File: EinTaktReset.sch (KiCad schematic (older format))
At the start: 59 parts, among them IC1 74LS624, J1 3PinTerminalBlocktg, J2 3PinTerminalBlocktg, P1 CONN_02X10, P4 CONN_02X10, SW1 SPST, SW10 SPST, SW11 SPST, SW12 SPST, SW13 SPST, SW2 SWITCH_INV, SW3 SPST, SW4 SPST, SW5 SPST, SW6 SWITCH_INV, SW7 SPST, SW8 SPST, SW9 SPST, U1 74LS132, U2 74540En, U3 74HCT541_PWR, U4 74LS32, U5 74LS00, U6 74LS132

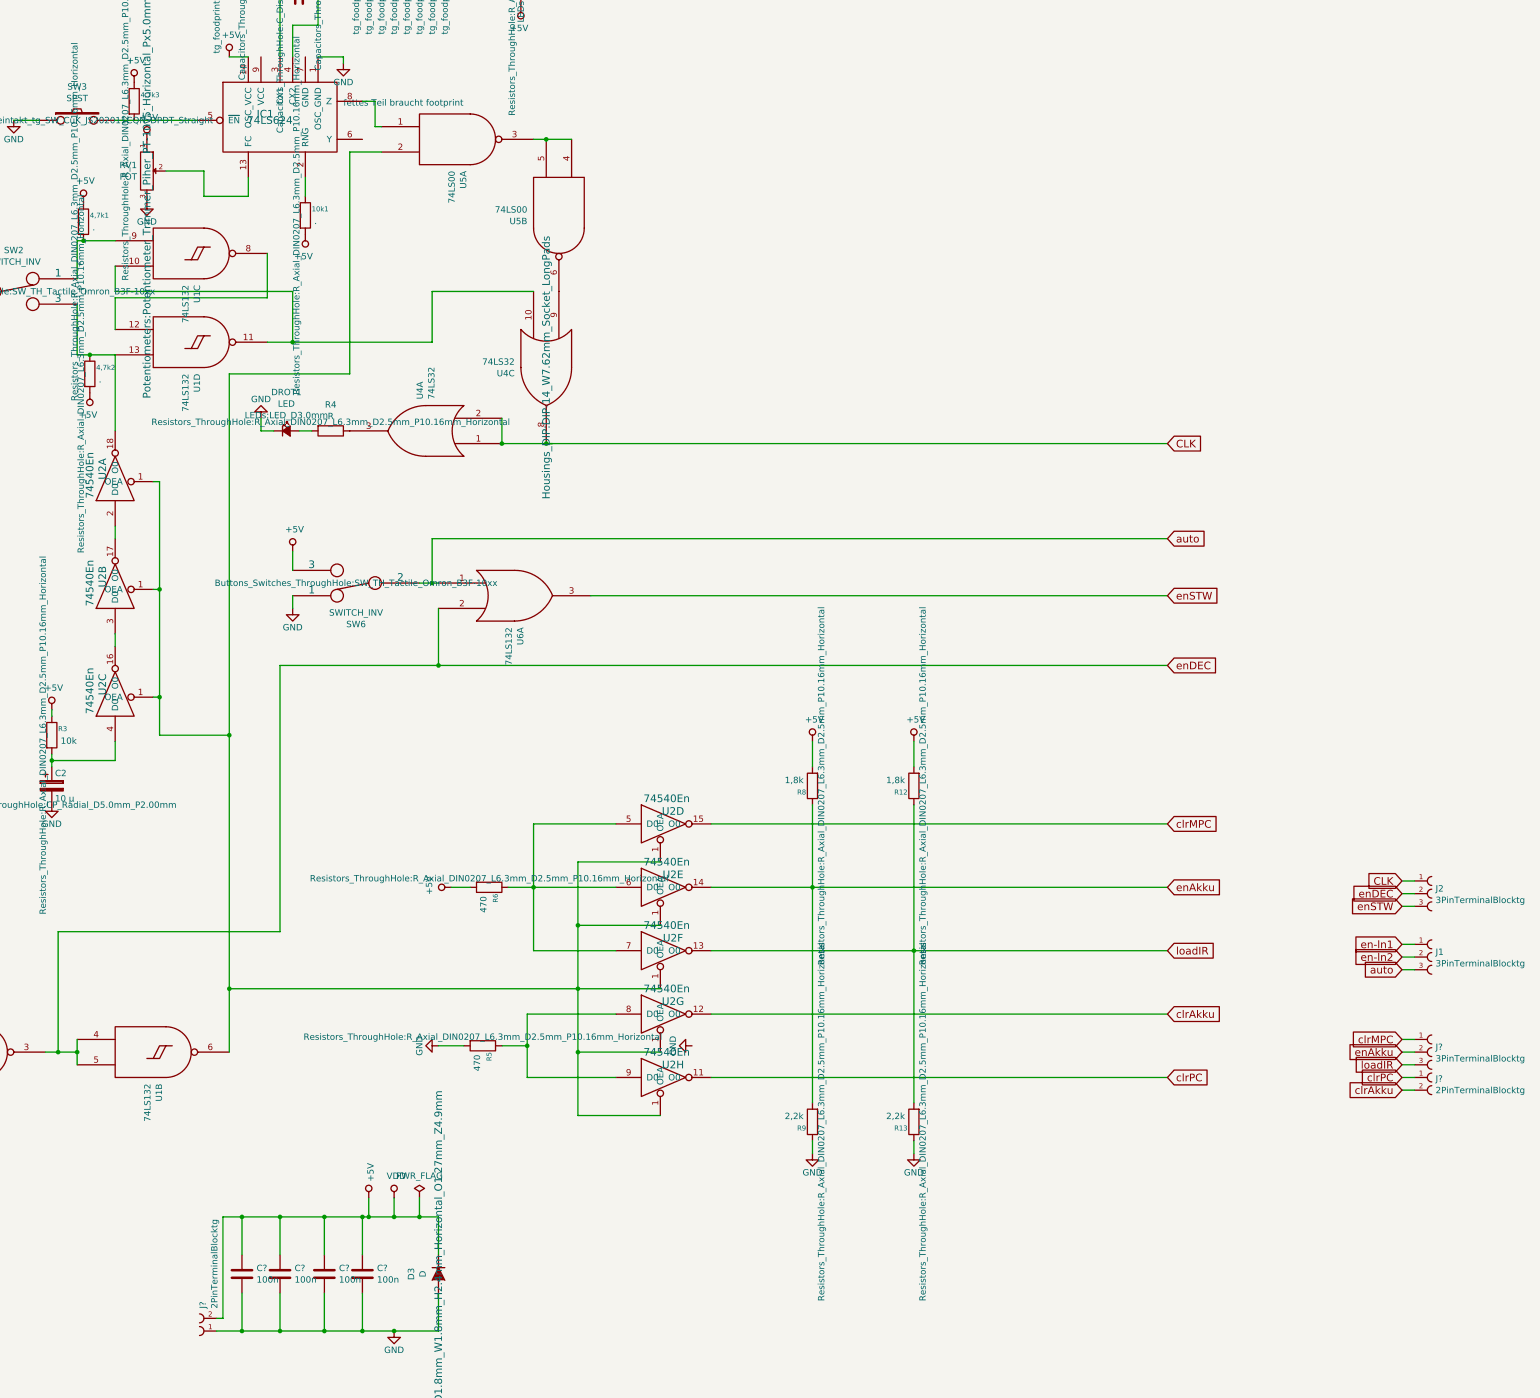
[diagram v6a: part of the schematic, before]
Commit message: pcb gelayoutet, Libraries benannt, todo.txt geändert!
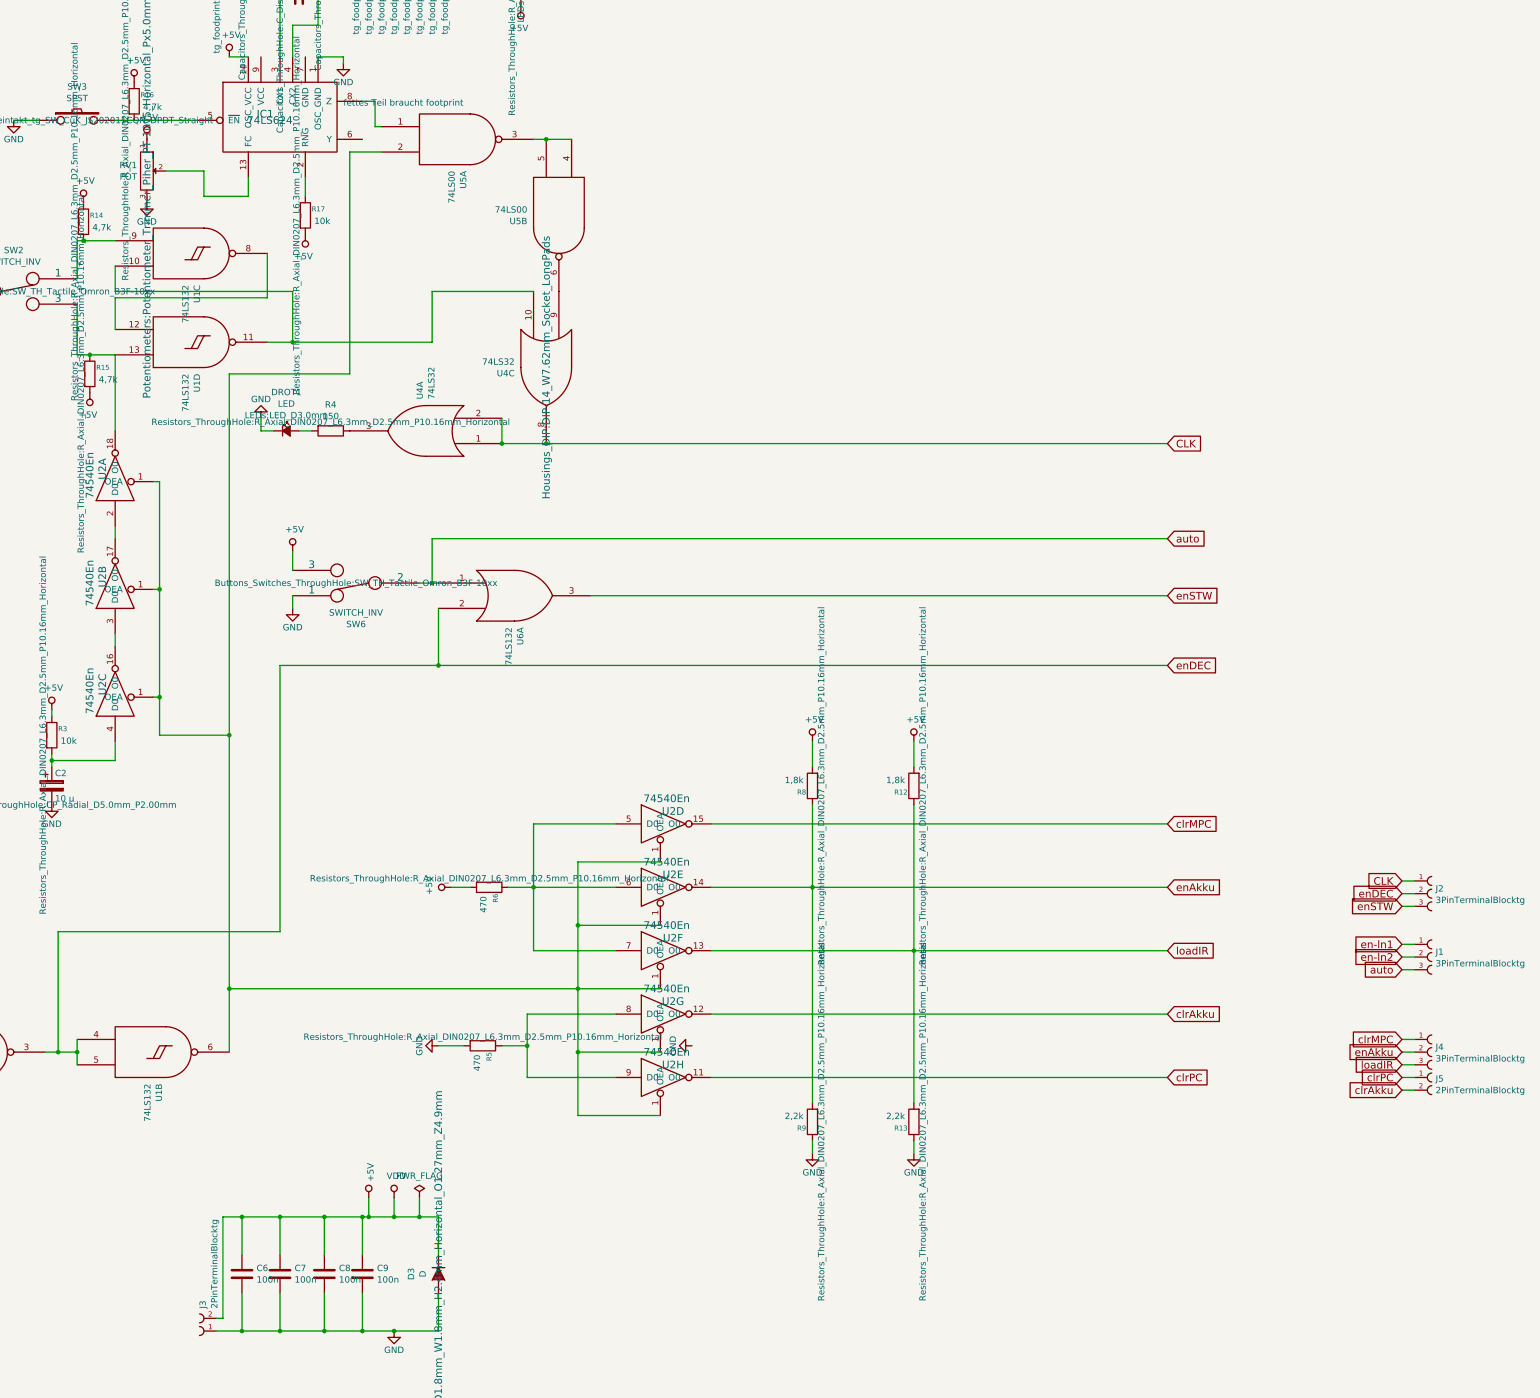
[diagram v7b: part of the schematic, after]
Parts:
- R14: renamed from 4,7k1; value . -> 4,7k
- R15: renamed from 4,7k2; value . -> 4,7k
- R16: renamed from 4,7k3; value . -> 4,7k
- R17: renamed from 10k1; value . -> 10k
- R4: value R -> 150
- gave numbers to parts that had none: 7
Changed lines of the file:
@@
 $EndComp
 $Comp
-L device:R 4,7k3
+L device:R R16
 U 1 1 5845B97A
 P 2500 5800
-F 0 "4,7k3" H 2550 5850 39  0000 L CNN
-F 1 "." H 2570 5755 50  0000 L CNN
+F 0 "R16" H 2550 5850 39  0000 L CNN
+F 1 "4,7k" H 2570 5755 50  0000 L CNN
 F 2 "Resistors_ThroughHole:R_Axial_DIN0207_L6.3mm_D2.5mm_P10.16mm_Horizontal" V 2430 5800 50  0000 C CNN
 F 3 "" H 2500 5800 50  0000 C CNN
@@
 $EndComp
 $Comp
-L device:R 10k1
+L device:R R17
 U 1 1 5845CFFB
 P 3850 6700
-F 0 "10k1" H 3900 6750 39  0000 L CNN
-F 1 "." H 3920 6655 50  0000 L CNN
+F 0 "R17" H 3900 6750 39  0000 L CNN
+F 1 "10k" H 3920 6655 50  0000 L CNN
 F 2 "Resistors_ThroughHole:R_Axial_DIN0207_L6.3mm_D2.5mm_P10.16mm_Horizontal" V 3780 6700 50  0000 C CNN
 F 3 "" H 3850 6700 50  0000 C CNN
@@
 $EndComp
 $Comp
-L device:R 4,7k2
+L device:R R15
 U 1 1 5845E30F
 P 2150 7950
-F 0 "4,7k2" H 2200 8000 39  0000 L CNN
-F 1 "." H 2220 7905 50  0000 L CNN
+F 0 "R15" H 2200 8000 39  0000 L CNN
+F 1 "4,7k" H 2220 7905 50  0000 L CNN
 F 2 "Resistors_ThroughHole:R_Axial_DIN0207_L6.3mm_D2.5mm_P10.16mm_Horizontal" V 2080 7950 50  0000 C CNN
 F 3 "" H 2150 7950 50  0000 C CNN
@@
 $EndComp
 $Comp
-L device:R 4,7k1
+L device:R R14
 U 1 1 5845F8A9
 P 2100 6750
-F 0 "4,7k1" H 2150 6800 39  0000 L CNN
-F 1 "." H 2170 6705 50  0000 L CNN
+F 0 "R14" H 2150 6800 39  0000 L CNN
+F 1 "4,7k" H 2170 6705 50  0000 L CNN
 F 2 "Resistors_ThroughHole:R_Axial_DIN0207_L6.3mm_D2.5mm_P10.16mm_Horizontal" V 2030 6750 50  0000 C CNN
 F 3 "" H 2100 6750 50  0000 C CNN
@@
 P 4050 8400
 F 0 "R4" V 3843 8400 50  0000 C CNN
-F 1 "R" V 3934 8400 50  0000 C CNN
+F 1 "150" V 3934 8400 50  0000 C CNN
 F 2 "Resistors_ThroughHole:R_Axial_DIN0207_L6.3mm_D2.5mm_P10.16mm_Horizontal" V 3980 8400 50  0000 C CNN
 F 3 "" H 4050 8400 50  0000 C CNN
@@
 	5750 8500 10650 8500
 $Comp
-L 2PinTerminalBlocktg:2PinTerminalBlocktg J?
+L 2PinTerminalBlocktg:2PinTerminalBlocktg J5
 U 1 1 5AC4DB91
 P 12800 13500
-F 0 "J?" H 12765 13490 50  0000 L CNN
+F 0 "J5" H 12765 13490 50  0000 L CNN
 F 1 "2PinTerminalBlocktg" H 12765 13399 50  0000 L CNN
 F 2 "2PinTerminalBlocktg" H 12800 13500 50  0001 L BNN
@@
 $EndComp
 $Comp
-L 3PinTerminalBlocktg:3PinTerminalBlocktg J?
+L 3PinTerminalBlocktg:3PinTerminalBlocktg J4
 U 1 1 5AC4DD64
 P 12800 13300
-F 0 "J?" H 12765 13340 50  0000 L CNN
+F 0 "J4" H 12765 13340 50  0000 L CNN
 F 1 "3PinTerminalBlocktg" H 12765 13249 50  0000 L CNN
 F 2 "3PinTerminalBlocktg" H 12800 13300 50  0001 L BNN
@@
 	12600 13600 12500 13600
 $Comp
-L 2PinTerminalBlocktg:2PinTerminalBlocktg J?
+L 2PinTerminalBlocktg:2PinTerminalBlocktg J3
 U 1 1 5ADB7E0E
 P 2950 15500
-F 0 "J?" V 2858 15323 50  0000 R CNN
+F 0 "J3" V 2858 15323 50  0000 R CNN
 F 1 "2PinTerminalBlocktg" V 2767 15323 50  0000 R CNN
 F 2 "2PinTerminalBlocktg" H 2950 15500 50  0001 L BNN
@@
 	4900 15500 4900 15200
 $Comp
-L bonsai:C C?
+L bonsai:C C9
 U 1 1 5AFD86A4
 P 4300 15050
-F 0 "C?" H 4415 15096 50  0000 L CNN
+F 0 "C9" H 4415 15096 50  0000 L CNN
 F 1 "100n" H 4415 15005 50  0000 L CNN
 F 2 "" H 4338 14900 30  0000 C CNN
@@
 $EndComp
 $Comp
-L bonsai:C C?
+L bonsai:C C8
 U 1 1 5AFEAAC4
 P 4000 15050
-F 0 "C?" H 4115 15096 50  0000 L CNN
+F 0 "C8" H 4115 15096 50  0000 L CNN
 F 1 "100n" H 4115 15005 50  0000 L CNN
 F 2 "" H 4038 14900 30  0000 C CNN
@@
 $EndComp
 $Comp
-L bonsai:C C?
+L bonsai:C C7
 U 1 1 5AFEABD4
 P 3650 15050
-F 0 "C?" H 3765 15096 50  0000 L CNN
+F 0 "C7" H 3765 15096 50  0000 L CNN
 F 1 "100n" H 3765 15005 50  0000 L CNN
 F 2 "" H 3688 14900 30  0000 C CNN
@@
 $EndComp
 $Comp
-L bonsai:C C?
+L bonsai:C C6
 U 1 1 5AFEACE5
 P 3350 15050
-F 0 "C?" H 3465 15096 50  0000 L CNN
+F 0 "C6" H 3465 15096 50  0000 L CNN
 F 1 "100n" H 3465 15005 50  0000 L CNN
 F 2 "" H 3388 14900 30  0000 C CNN

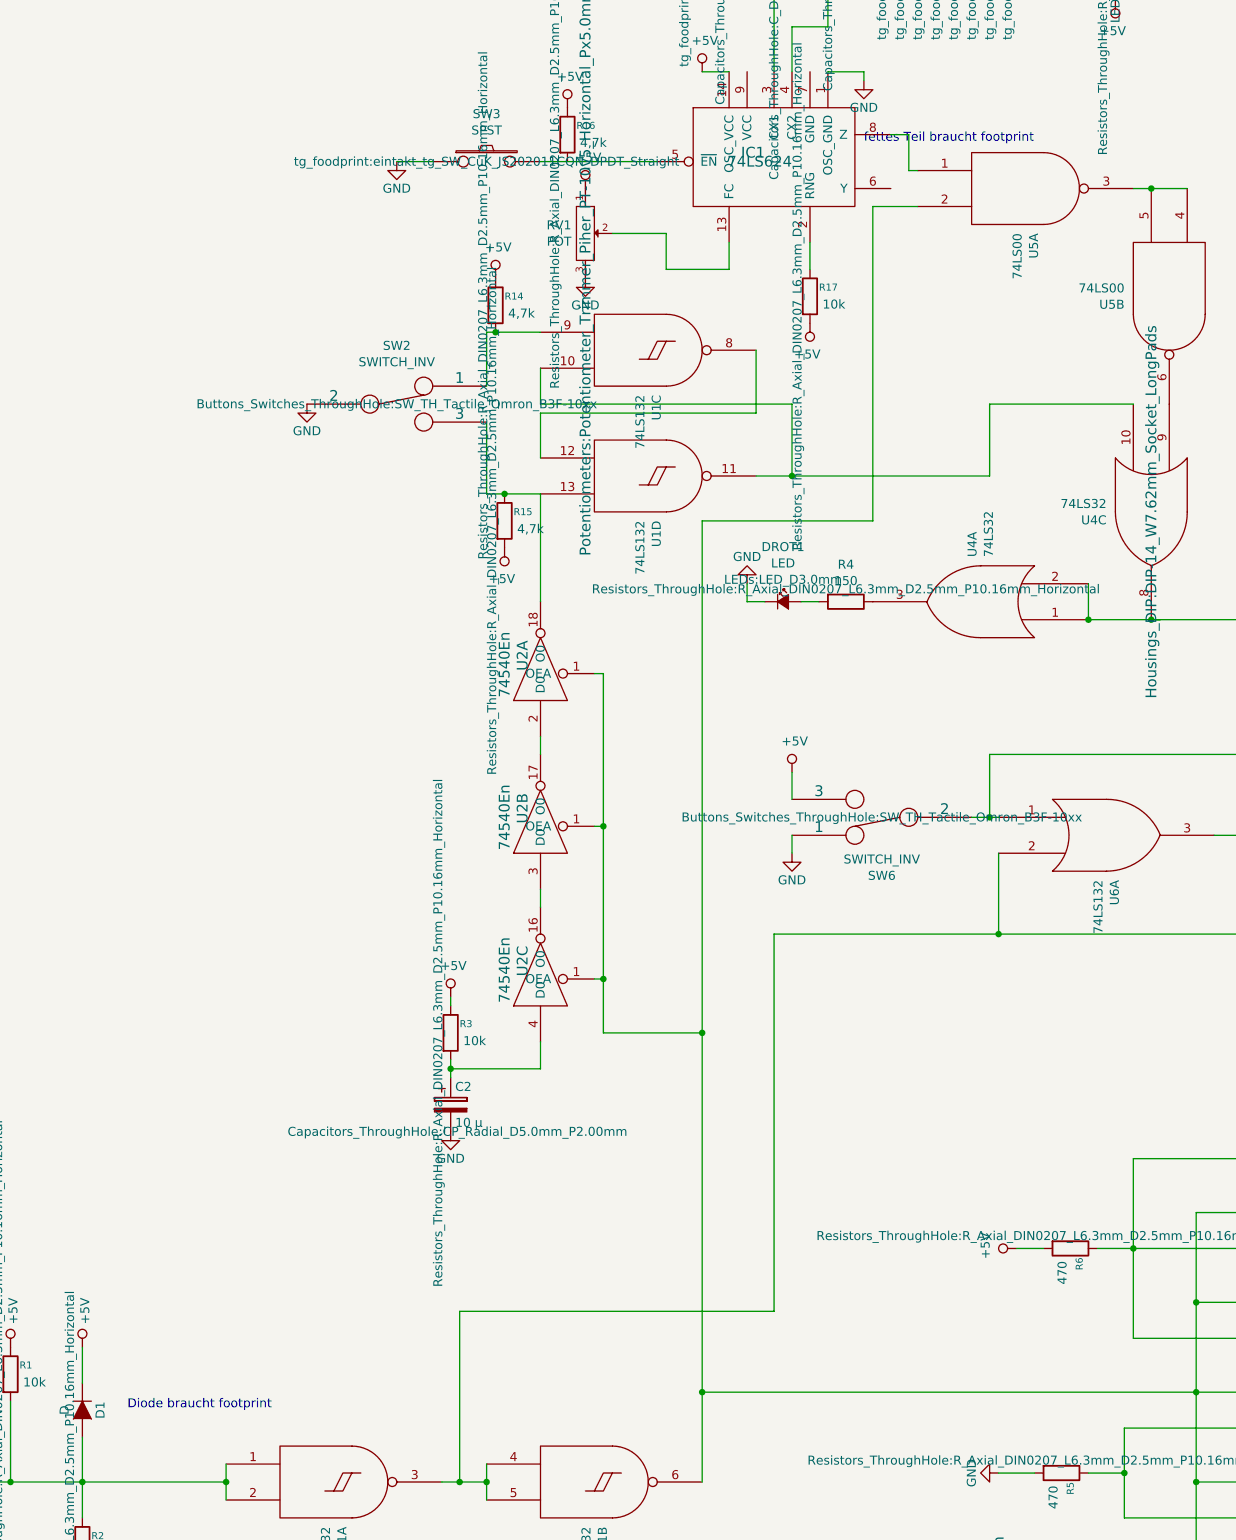
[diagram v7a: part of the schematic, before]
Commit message: todo aktualisiert und gelayoutet
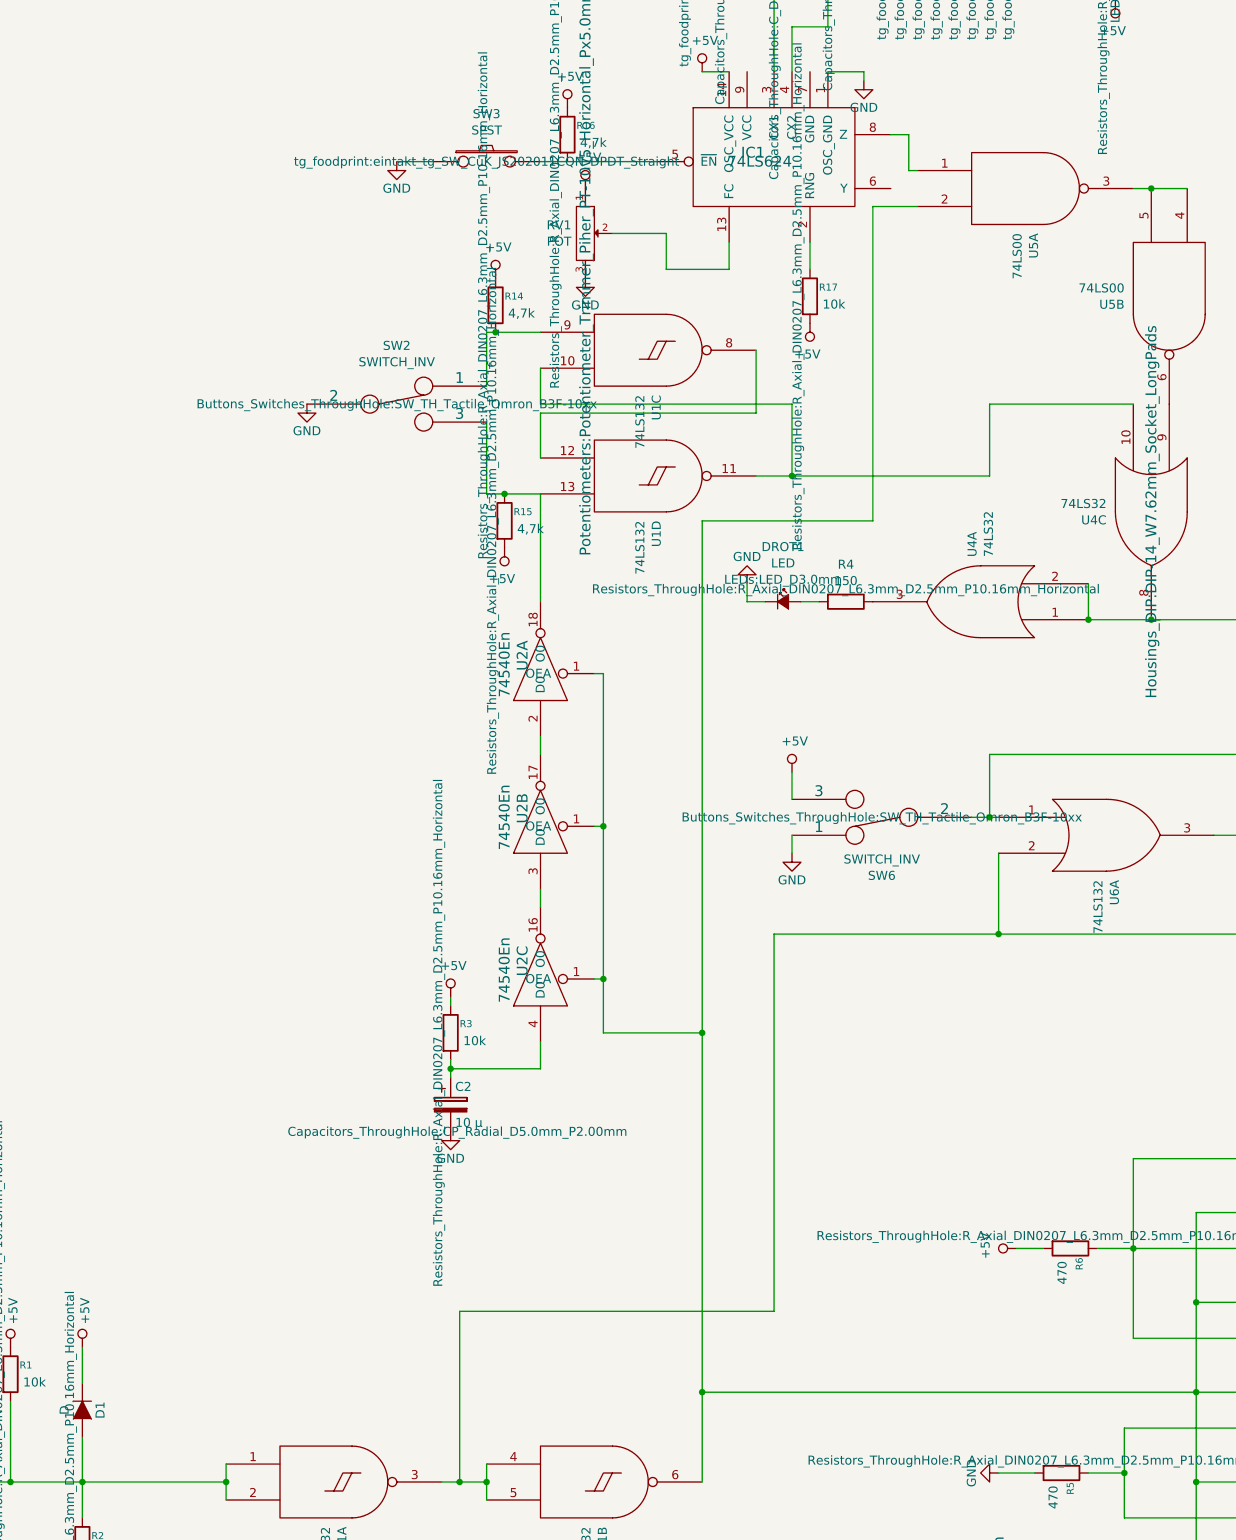
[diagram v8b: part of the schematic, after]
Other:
- note removed: "Diode braucht footprint\n"
- note removed: "fettes Teil braucht footprint"
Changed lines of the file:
@@
 	0    1    1    0
 $EndComp
-Text Notes 50   12900 0    50   ~ 0
-Diode braucht footprint\n
-Text Notes 4150 5850 0    50   ~ 0
-fettes Teil braucht footprint
 $Comp
 L vco:74LS624 IC1
